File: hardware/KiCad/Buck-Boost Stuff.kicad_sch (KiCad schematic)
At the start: 73 parts, among them Q5 CSD19505KCS, Q6 CSD19505KCS, Q7 CSD19505KCS, Q8 CSD19505KCS, U2 B1212S-1W_C883463, U3 B1212S-1W_C883463, U4 INA240A4DR, U5 INA240A4DR, U6 ACS712ELCTR-30A-T, U7 ACS712ELCTR-30A-T

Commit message: feat(hardware): initialize v1.3 roadmap, standards, and phase 1 power stage optimization
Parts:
- R11, R12, R37, R38: value 10Ω -> 5.1Ω
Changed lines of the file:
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@@
 			)
 		)
-		(property "Value" "10Ω"
+		(property "Value" "5.1Ω"
 			(at 96.2914 172.0469 0)
 			(show_name no)
@@
 			)
 		)
-		(property "Value" "10Ω"
+		(property "Value" "5.1Ω"
 			(at 234.7214 156.8069 0)
 			(show_name no)
@@
 			)
 		)
-		(property "Value" "10Ω"
+		(property "Value" "5.1Ω"
 			(at 234.7214 127.5969 0)
 			(show_name no)
@@
 			)
 		)
-		(property "Value" "10Ω"
+		(property "Value" "5.1Ω"
 			(at 96.2914 142.8369 0)
 			(show_name no)

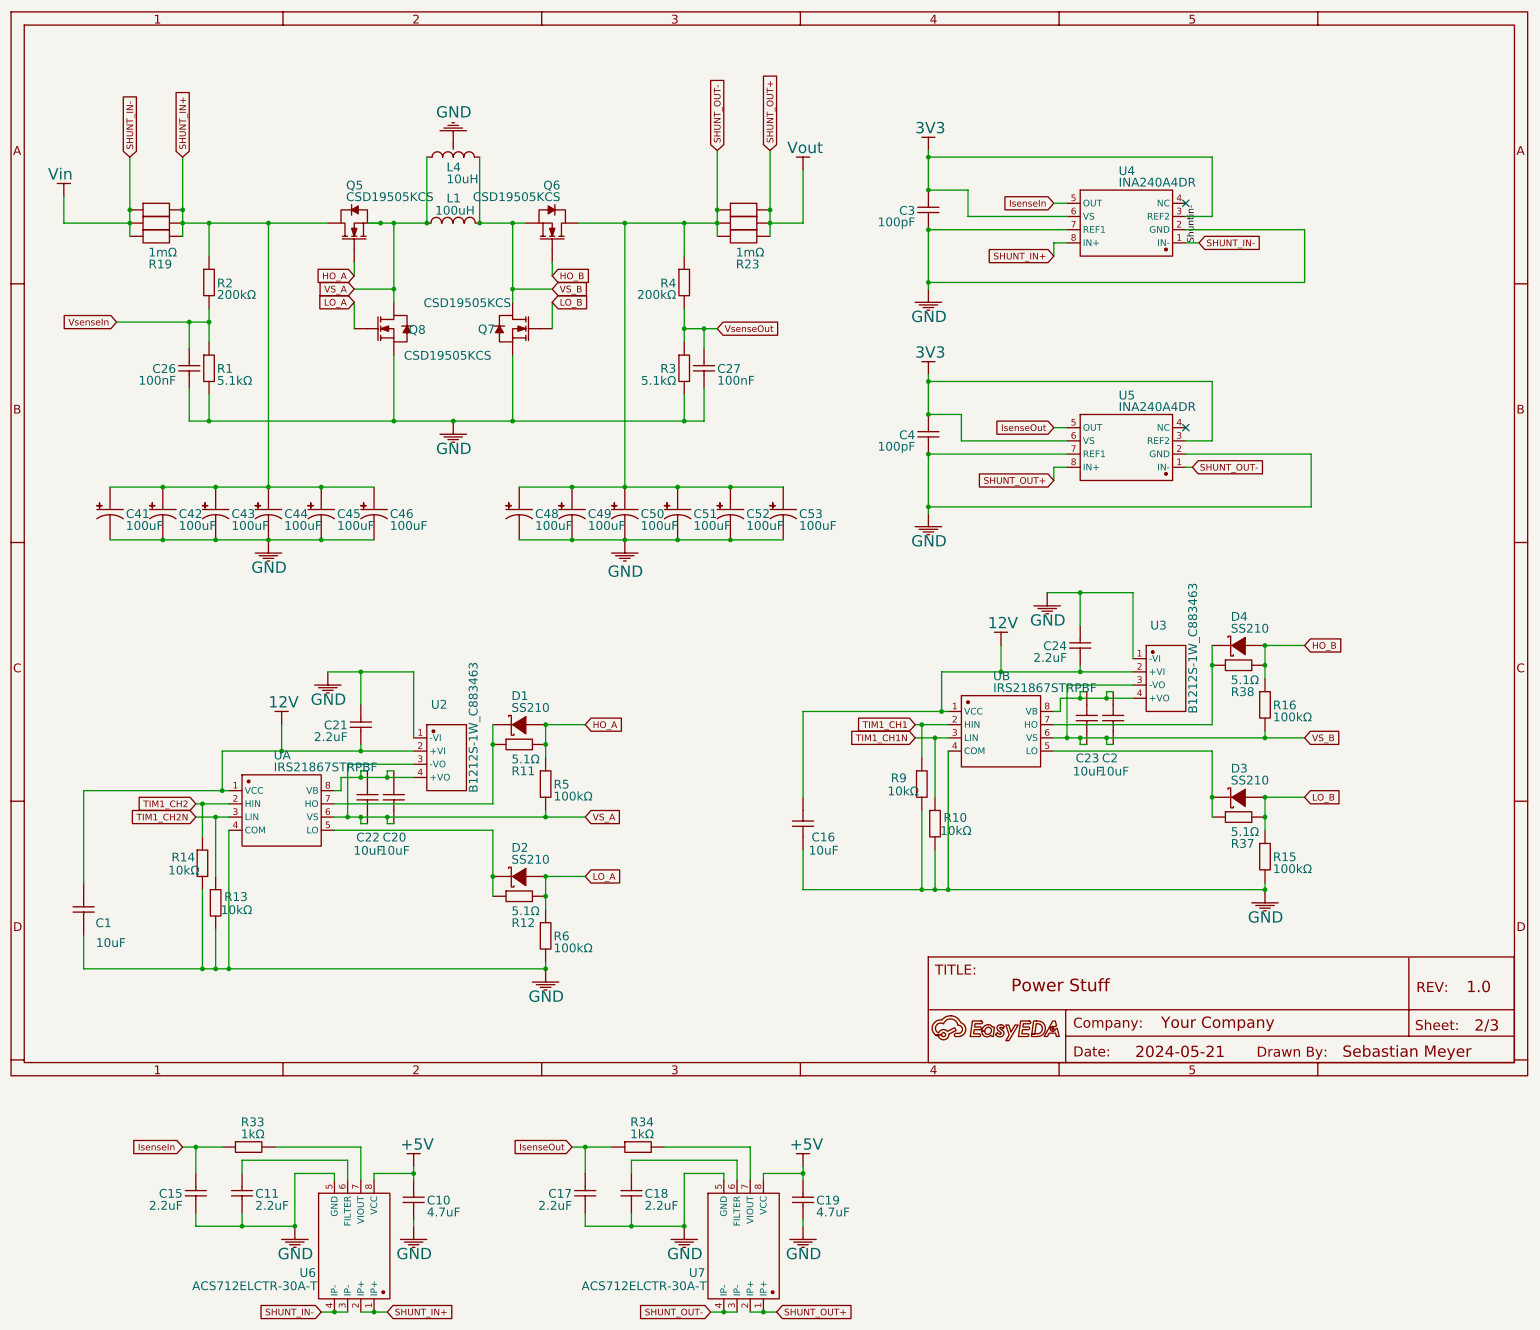
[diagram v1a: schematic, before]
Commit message: added the new 10v regulator
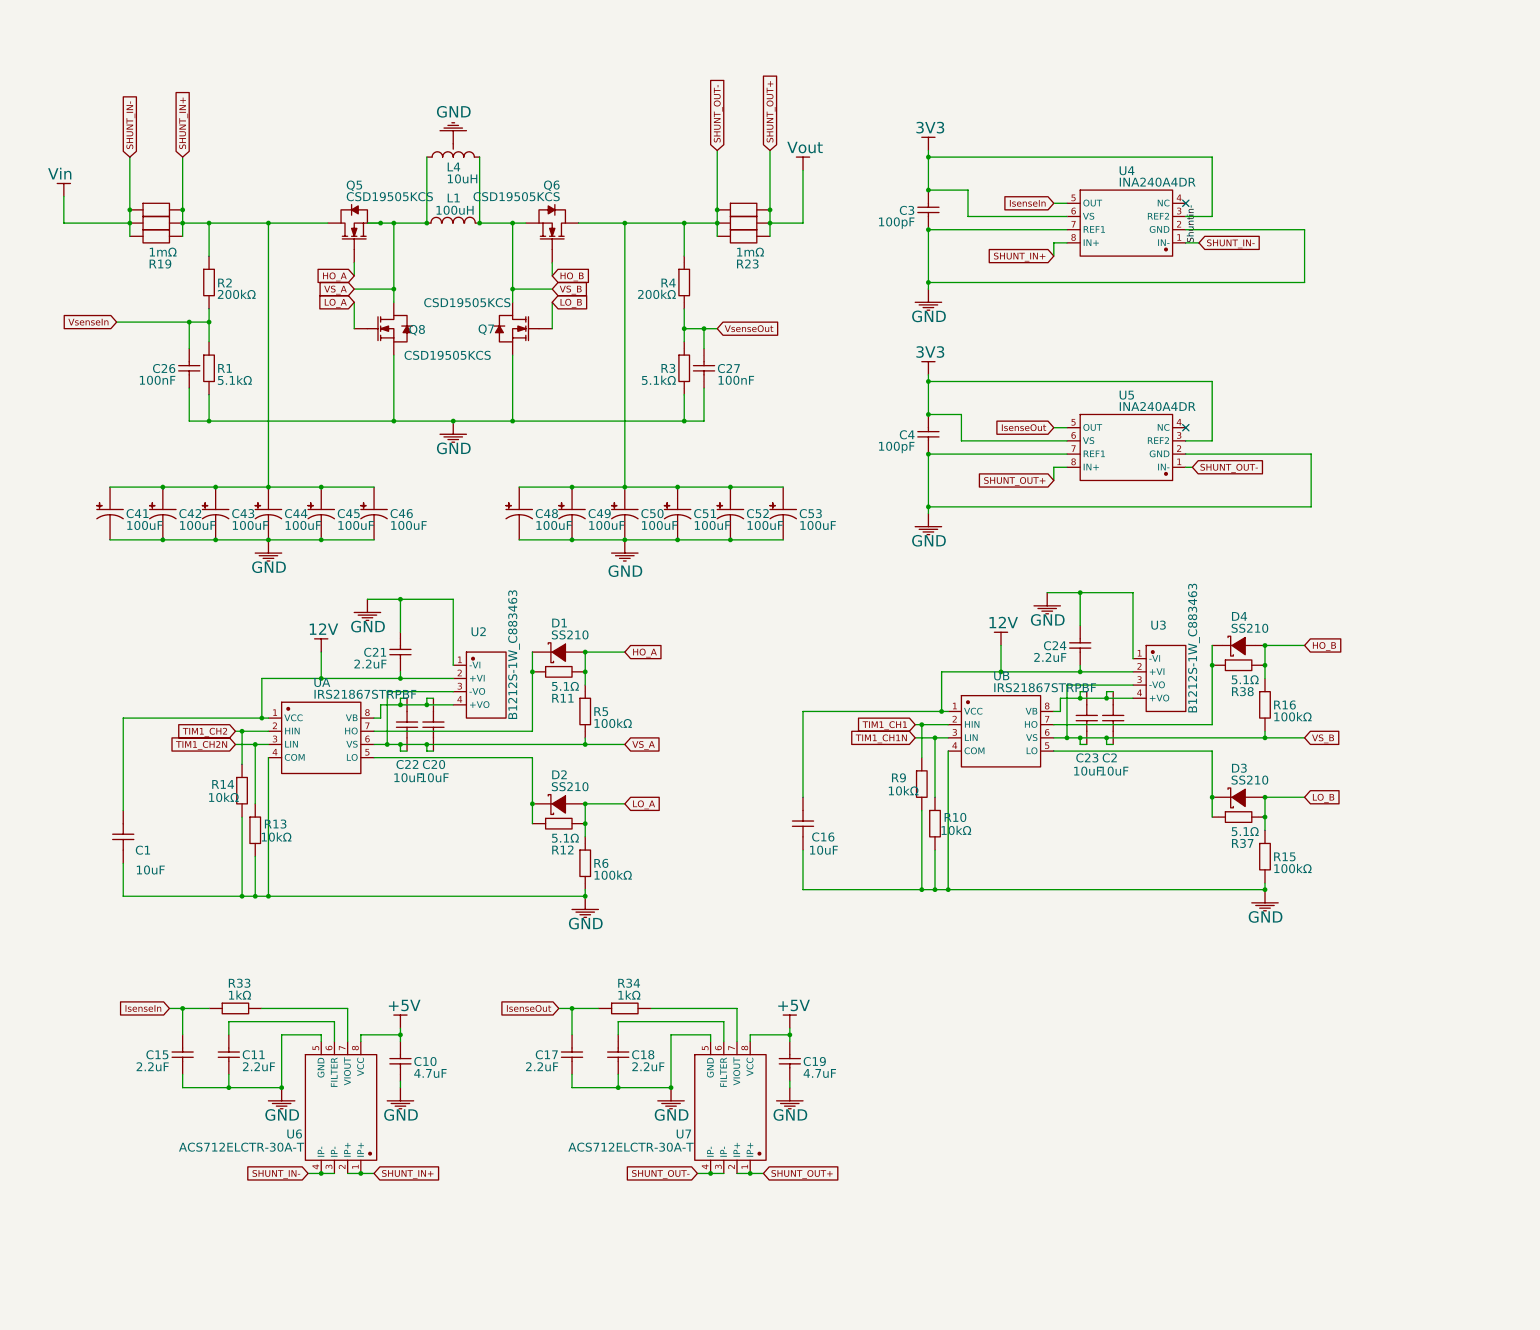
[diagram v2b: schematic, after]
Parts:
- removed A: A, symbol Unknown_15_-845
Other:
- moved on the sheet: C1, C10, C11, C15, C17, C18, C19, C20, C21, C22, D1, D2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

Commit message: added 3v3 regulator
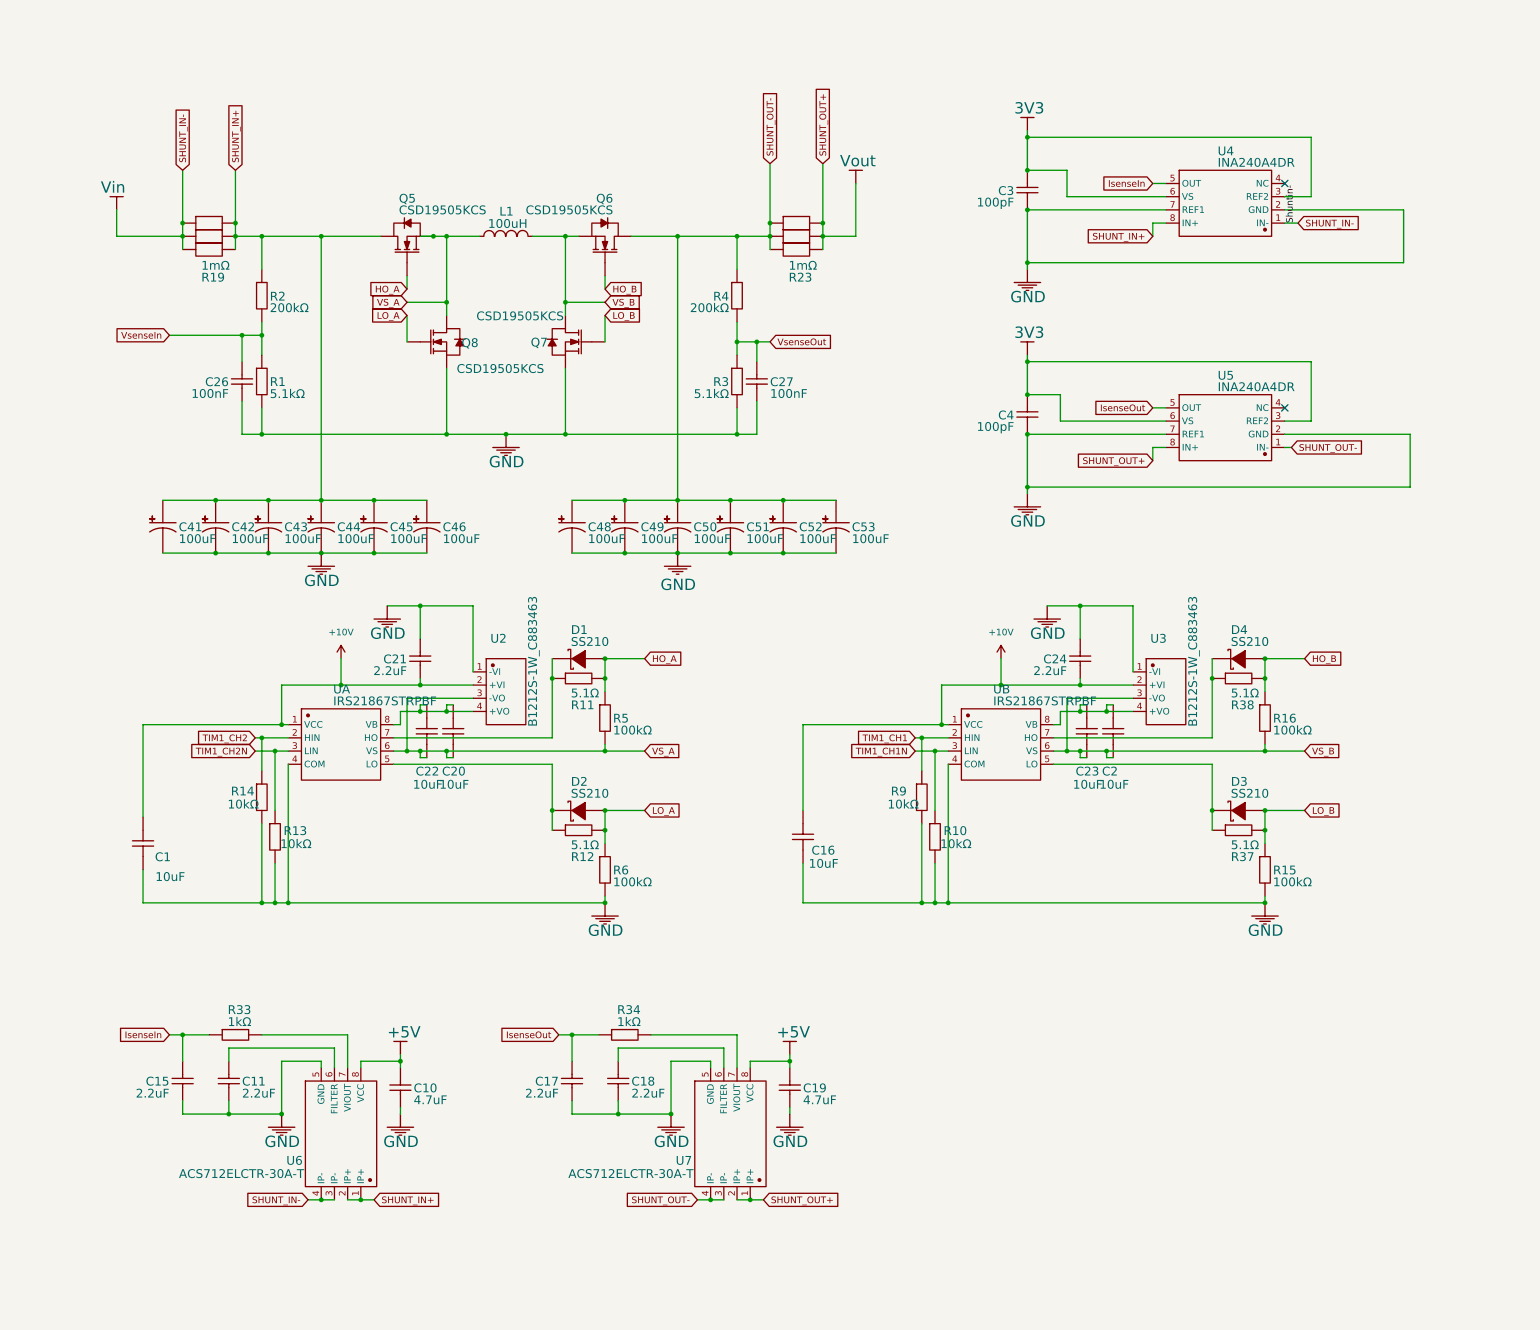
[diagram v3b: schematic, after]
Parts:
- removed L4: 10uH, symbol FC-SE2918-100M-28A
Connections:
- net 12V renamed +10V
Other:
- moved on the sheet: C1, C10, C11, C15, C16, C17, C18, C19, C2, C20, C21, C22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
